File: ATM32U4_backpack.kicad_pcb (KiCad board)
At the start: 2 copper layers, 27 x 50.5 mm, 41 parts, among them J1 ISP, J2 WS2812, J3 UART, J4 USB_B_Micro, J5 OLED, J6 ENC, U1 LM3480-3.3, U3 NTS0101GW, U4 ATmega32U4-AU, Y1 16MHz

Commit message: Added License and expanded gitignore
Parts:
- TP4: value Ar -> AREF
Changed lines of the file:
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@@
     (solder_mask_min_width 0.25)
     (aux_axis_origin 0 0)
-    (visible_elements FFFFFF7F)
+    (visible_elements 7FFFFFFF)
     (pcbplotparams
       (layerselection 0x010fc_ffffffff)
@@
       (effects (font (size 1 1) (thickness 0.15)) (justify mirror))
     )
-    (fp_text value Ar (at 0 -1.5 90) (layer B.SilkS)
+    (fp_text value AREF (at 0 -1.5 90) (layer B.SilkS)
       (effects (font (size 1 1) (thickness 0.15)) (justify mirror))
     )

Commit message: added schematic pdf and readme
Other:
- board text added: "1"
- board text added: "5"
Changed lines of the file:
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@@
   (general
     (thickness 1.6)
-    (drawings 4)
+    (drawings 6)
     (tracks 440)
     (zones 0)
@@
     )
   )
+  (gr_text 5 (at 47.9 115.6) (layer F.SilkS)
+    (effects (font (size 1 1) (thickness 0.15)))
+  )
+  (gr_text 1 (at 47.9 110.5) (layer F.SilkS)
+    (effects (font (size 1 1) (thickness 0.15)))
+  )
   (gr_line (start 57 120.5) (end 30 120.5) (layer Edge.Cuts) (width 0.05))

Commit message: Added gerbers
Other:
- board text added: "ATMega32U4 BackPack Rev1.0.0 git.io/AVRBP"
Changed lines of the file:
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@@
   (general
     (thickness 1.6)
-    (drawings 6)
+    (drawings 8)
     (tracks 440)
     (zones 0)
@@
     (visible_elements 7FFFFFFF)
     (pcbplotparams
-      (layerselection 0x010fc_ffffffff)
+      (layerselection 0x010f0_ffffffff)
       (usegerberextensions false)
       (usegerberattributes false)
@@
       (outputformat 1)
       (mirror false)
-      (drillshape 1)
+      (drillshape 0)
       (scaleselection 1)
-      (outputdirectory ""))
+      (outputdirectory "gerbers/"))
   )
   (net 0 "")
@@
     (tags SOD-323)
     (attr smd)
-    (fp_text reference D1 (at -2.7 0 180) (layer F.SilkS)
+    (fp_text reference D1 (at 2.7 0 180) (layer F.SilkS)
       (effects (font (size 1 1) (thickness 0.15)))
     )
@@
     )
   )
+  (gr_text "ATMega32U4 BackPack\nRev1.0.0\ngit.io/AVRBP" (at 48.2 93.4 270) (layer B.SilkS)
+    (effects (font (size 1.3 1.3) (thickness 0.25)) (justify left mirror))
+  )
+  (gr_text "ATMega32U4 BackPack\nRev1.0.0\ngit.io/AVRBP" (at 33.8 93.6 90) (layer F.SilkS)
+    (effects (font (size 1.3 1.3) (thickness 0.25)) (justify left))
+  )
   (gr_text 5 (at 47.9 115.6) (layer F.SilkS)

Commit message: Fixed back silkscreen
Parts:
- TP4: value AREF -> Ar
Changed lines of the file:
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@@
       (effects (font (size 1 1) (thickness 0.15)) (justify mirror))
     )
-    (fp_text value AREF (at 0 -1.5 90) (layer B.SilkS)
+    (fp_text value Ar (at 0 -1.5 90) (layer B.SilkS)
       (effects (font (size 1 1) (thickness 0.15)) (justify mirror))
     )
@@
     )
   )
-  (gr_text "ATMega32U4 BackPack\nRev1.0.0\ngit.io/AVRBP" (at 48.2 93.4 270) (layer B.SilkS)
+  (gr_text "ATMega32U4 \nBackPack\nRev1.0.0\ngit.io/AVRBP" (at 47.4 115.4) (layer B.SilkS)
     (effects (font (size 1.3 1.3) (thickness 0.25)) (justify left mirror))
   )

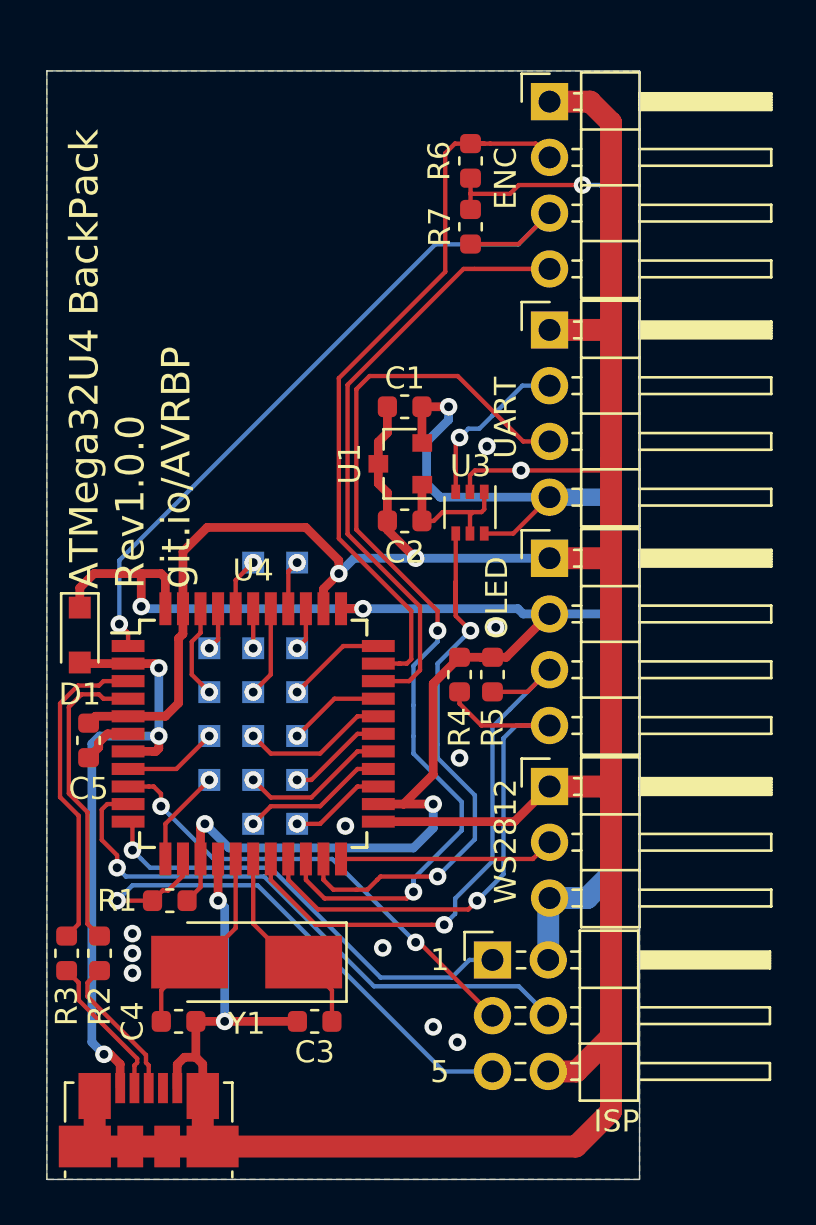
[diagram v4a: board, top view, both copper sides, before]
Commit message: Made SPI level-shifted to 3v3
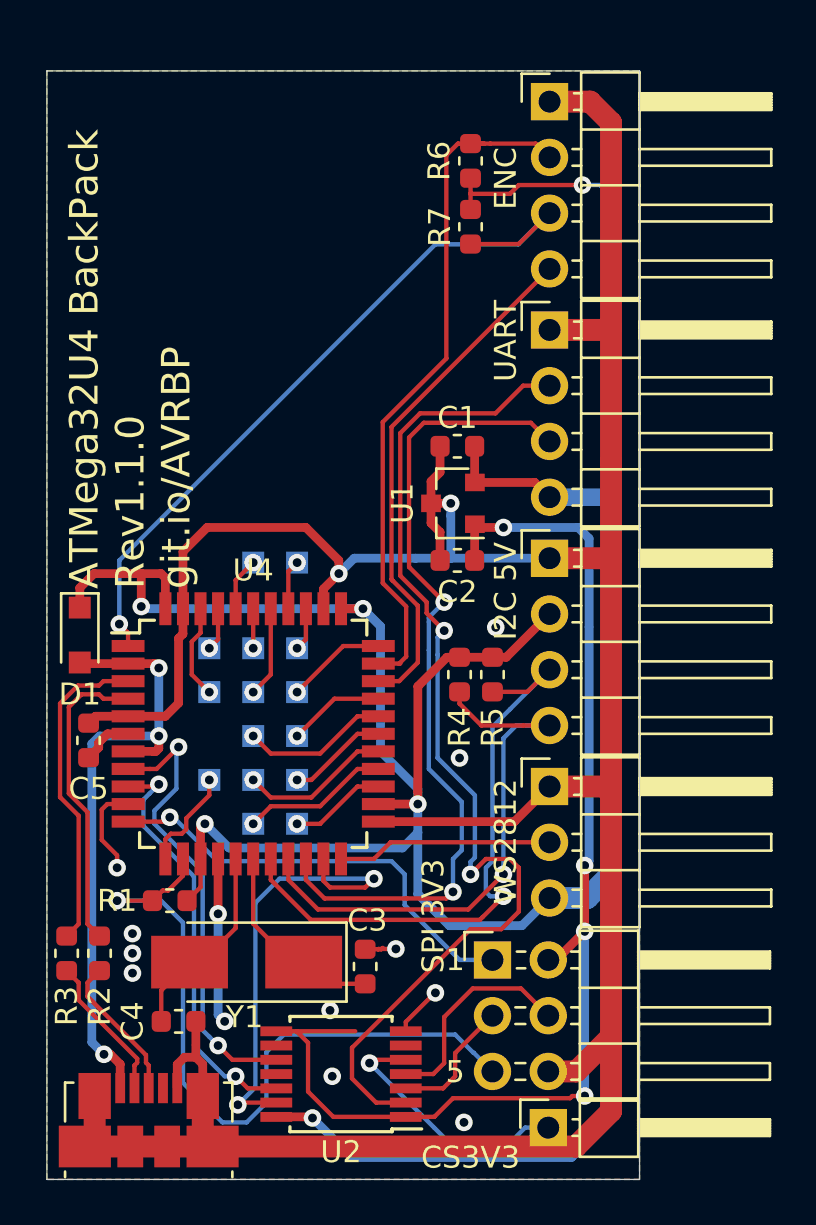
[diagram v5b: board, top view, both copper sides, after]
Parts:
- removed TP15: F6, TestPoint:TestPoint_Pad_1.0x1.0mm
- removed U3: NTS0101GW, Package_TO_SOT_SMD:SOT-363_SC-70-6
- added J7: CS3V3, Connector_PinHeader_2.54mm:PinHeader_1x01_P2.54mm_Horizontal, F.Cu at (52.8, 118.1)
- added U2: TXB0104PW, Package_SO:TSSOP-14_4.4x5mm_P0.65mm, F.Cu at (43.4, 115.7)
- J1: value ISP -> SPI 3V3
- J5: value OLED -> I2C 5V
- TP1: value B0 -> F6
- moved TP1 8.85 mm to (41.4, 92.4), turned to 180 degrees
- moved C3 3.40 mm to (44.5, 110.8), turned to 90 degrees
- moved C1 3.00 mm to (48.7, 87.1)
- moved C2 3.00 mm to (48.7, 92.3)
- moved U1 3.00 mm to (48.5, 89.7)
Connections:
- J1 pad 2: +5V -> +3V3
- J1 pad 3: /SCK -> /SCK-3V3
- J1 pad 4: /MOSI -> /MOSI-3V3
- U4 pad 10: /MOSI -> (no net)
- U4 pad 37: Net-(TP15-Pad1) -> Net-(TP1-Pad1)
- U4 pad 8: Net-(TP1-Pad1) -> /CS-5V
- U4 pad 9: /SCK -> /SCK-5V
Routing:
- net +3V3: track 6.57 -> 54.8 mm, vias 0 -> 4
- net /TX-3V3: track 7.66 -> 48.7 mm, vias 1 -> 2
- net /MOSI: track 26.7 -> 0.00 mm, vias 1 -> 0
- net +5V: track 126.3 -> 149.8 mm
- net /SCK: track 21.3 -> 0.00 mm, vias 2 -> 0
- net /CS-5V: track 0.00 -> 20.9 mm, vias 0 -> 2
- net /SCK-5V: track 0.00 -> 19.1 mm, vias 0 -> 2
- net /CS-3V3: track 0.00 -> 11.6 mm, vias 0 -> 1
- net /MOSI-3V3: track 0.00 -> 9.85 mm
- net /~Reset: track 25.1 -> 33.5 mm
- net GND: track 170.3 -> 163.1 mm, vias 15 -> 14
- net /RX-3V3: track 43.9 -> 37.6 mm
- net /SCK-3V3: track 0.00 -> 5.94 mm
- net /TX-5V: track 25.9 -> 20.8 mm
- net /ENC_SW: track 27.9 -> 23.6 mm
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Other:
- board text added: "ATMega32U4 BackPack Rev1.1.0 git.io/AVRBP"
- board text removed: "ATMega32U4 BackPack Rev1.0.0 git.io/AVRBP"
